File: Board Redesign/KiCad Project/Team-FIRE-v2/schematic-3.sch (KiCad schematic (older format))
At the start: 6 parts, among them IC2 BTS500601TEAAUMA2, J6 U.FL-R-SMT_10_, J7 132136RP, U6 MCP1826T-3302E_DC, U8 TPS82140SILR

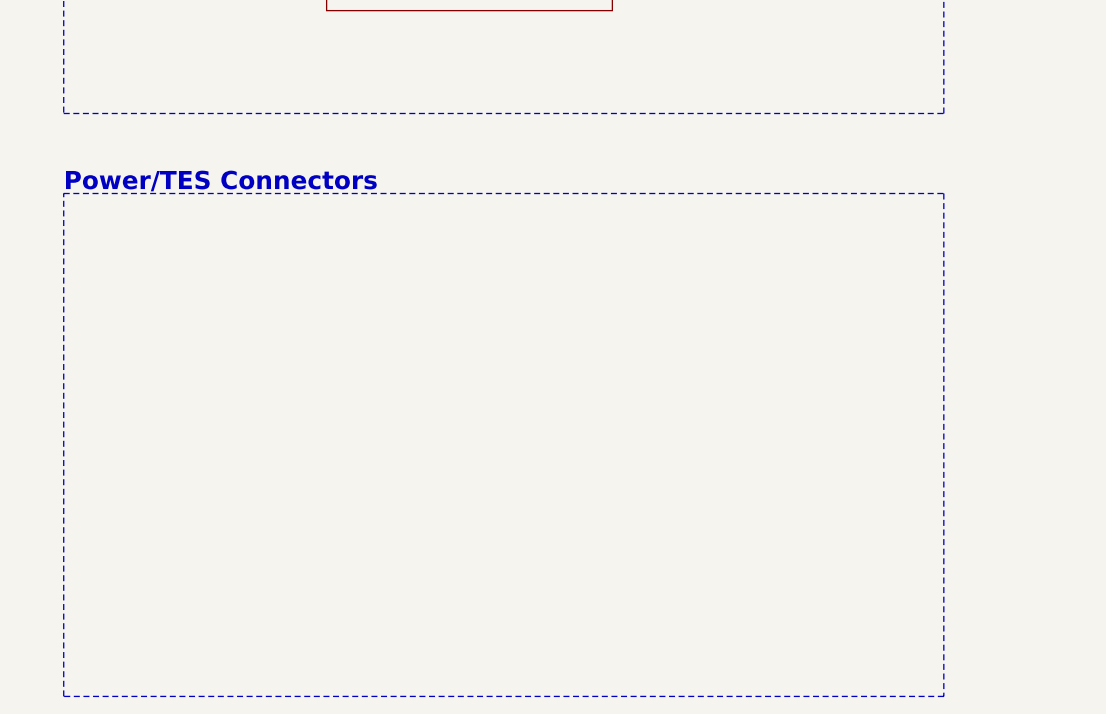
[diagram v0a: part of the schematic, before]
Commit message: Added TES connector
- Added the two 1x3 connectors to page 3 of the schematic
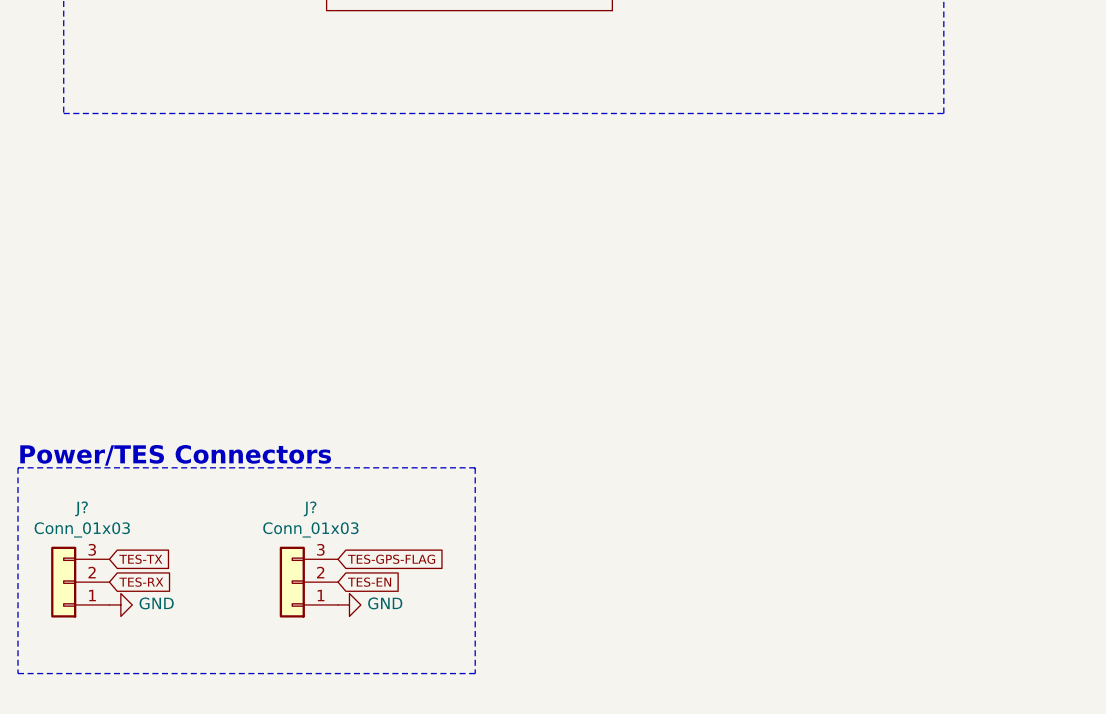
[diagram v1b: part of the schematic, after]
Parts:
- added J? (x2): Conn_01x03, Connector_JST:JST_SH_SM03B-SRSS-TB_1x03-1MP_P1.00mm_Horizontal, symbol Connector_Generic:Conn_01x03
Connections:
- net labels added: TES-EN, TES-GPS-FLAG, TES-RX, TES-TX
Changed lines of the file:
@@
 EESchema Schematic File Version 4
+LIBS:Team-FIRE-v2-cache
 EELAYER 30 0
 EELAYER END
@@
 Text Notes 1050 1000 0    79   ~ 16
 Iridium 8V PMIC
-Wire Notes Line
-	1050 5300 4900 5300
-Wire Notes Line
-	4900 5300 4900 7500
-Wire Notes Line
-	4900 7500 1050 7500
-Wire Notes Line
-	1050 7500 1050 5300
-Text Notes 1050 5300 0    79   ~ 16
+Text Notes 850  6500 0    79   ~ 16
 Power/TES Connectors
 Wire Notes Line
@@
 	1    0    0    -1
 $EndComp
+$Comp
+L Connector_Generic:Conn_01x03 J?
+U 1 1 5EA3E857
+P 1050 7000
+F 0 "J?" H 968 6675 50  0000 C CNN
+F 1 "Conn_01x03" H 968 6766 50  0000 C CNN
+F 2 "Connector_JST:JST_SH_SM03B-SRSS-TB_1x03-1MP_P1.00mm_Horizontal" H 1050 7000 50  0001 C CNN
+F 3 "~" H 1050 7000 50  0001 C CNN
+F 4 "SM03B-SRSS-TB(LF)(SN)" H 1050 7000 50  0001 C CNN "MPN"
+	1    1050 7000
+	-1   0    0    1
+$EndComp
+$Comp
+L Connector_Generic:Conn_01x03 J?
+U 1 1 5EA3FD2C
+P 2050 7000
+F 0 "J?" H 1968 6675 50  0000 C CNN
+F 1 "Conn_01x03" H 1968 6766 50  0000 C CNN
+F 2 "Connector_JST:JST_SH_SM03B-SRSS-TB_1x03-1MP_P1.00mm_Horizontal" H 2050 7000 50  0001 C CNN
+F 3 "~" H 2050 7000 50  0001 C CNN
+F 4 "SM03B-SRSS-TB(LF)(SN)" H 2050 7000 50  0001 C CNN "MPN"
+	1    2050 7000
+	-1   0    0    1
+$EndComp
+Text GLabel 1250 6900 2    39   Input ~ 0
+TES-TX
+Text GLabel 1250 7000 2    39   Input ~ 0
+TES-RX
+$Comp
+L power:GND #PWR?
+U 1 1 5EA4D0AF
+P 1250 7100
+F 0 "#PWR?" H 1250 6850 50  0001 C CNN
+F 1 "GND" V 1255 6972 50  0000 R CNN
+F 2 "" H 1250 7100 50  0001 C CNN
+F 3 "" H 1250 7100 50  0001 C CNN
+	1    1250 7100
+	0    -1   -1   0
+$EndComp
+Text GLabel 2250 6900 2    39   Input ~ 0
+TES-GPS-FLAG
+Text GLabel 2250 7000 2    39   Input ~ 0
+TES-EN
+$Comp
+L power:GND #PWR?
+U 1 1 5EA5A5FD
+P 2250 7100
+F 0 "#PWR?" H 2250 6850 50  0001 C CNN
+F 1 "GND" V 2255 6972 50  0000 R CNN
+F 2 "" H 2250 7100 50  0001 C CNN
+F 3 "" H 2250 7100 50  0001 C CNN
+	1    2250 7100
+	0    -1   -1   0
+$EndComp
+Wire Notes Line
+	850  6500 2850 6500
+Wire Notes Line
+	850  7400 2850 7400
+Wire Notes Line
+	850  6500 850  7400
+Wire Notes Line
+	2850 6500 2850 7400
 $EndSCHEMATC

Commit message: Finished RF Connector
- Deleted old 132136RP antenna connector
- Added new MMCX antenna connector footprint, symbol, and 3D model
- Added MMCX antenna and U.FL connector to Schematic Page 3
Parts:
- removed J6: U.FL-R-SMT_10_, UFLRSMT10, symbol Team-FIRE:U.FL-R-SMT_10_
- removed J7: 132136RP, 132136RP, symbol Team-FIRE:132136RP
- added J?: U.FL-R-SMT_10_, Team-FIRE:UFLRSMT10, symbol Team-FIRE:U.FL-R-SMT_10_
- added J?: PCB.MMCX.F.ST.SMT.JACK.HT, Team-FIRE:PCBMMCXFSTSMTJACKHT, symbol Team-FIRE:PCB.MMCX.F.ST.SMT.JACK.HT
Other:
- note added: "Antenna Connector\n"
- note added: "IRIDIUM U.FL Connector"
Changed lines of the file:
@@
 EESchema Schematic File Version 4
-LIBS:Team-FIRE-v2-cache
 EELAYER 30 0
 EELAYER END
 $Descr A4 11693 8268
 encoding utf-8
-Sheet 4 4
+Sheet 1 1
 Title "Team FIRE Flight-Ready Iridium Carrier"
 Date "2020-02-24"
@@
 Comment4 "Koffi Anderson, Collin Heist, Shelby Linafelter"
 $EndDescr
-Wire Notes Line
-	8250 4750 8250 6050
-Wire Notes Line
-	10850 6050 10850 4750
-Text Notes 8300 4750 0    79   ~ 16
+Text Notes 8350 5200 0    79   ~ 16
 RF Connector
 Text Notes 6850 850  0    79   ~ 16
@@
 Wire Notes Line
 	10700 850  6850 850
-Wire Wire Line
-	9800 5550 9700 5550
-Wire Wire Line
-	9700 5550 9700 5650
-Wire Wire Line
-	9700 5650 9800 5650
-Wire Wire Line
-	9700 5650 9700 5750
-Connection ~ 9700 5650
-Wire Wire Line
-	10600 5450 10700 5450
-Wire Wire Line
-	10700 5450 10700 5550
-Wire Wire Line
-	10600 5550 10700 5550
-Connection ~ 10700 5550
-Wire Wire Line
-	10700 5550 10700 5650
-$Comp
-L power:GND #PWR0152
-U 1 1 5EA5E592
-P 10700 5650
-F 0 "#PWR0152" H 10700 5400 50  0001 C CNN
-F 1 "GND" H 10705 5477 50  0000 C CNN
-F 2 "" H 10700 5650 50  0001 C CNN
-F 3 "" H 10700 5650 50  0001 C CNN
-	1    10700 5650
-	1    0    0    -1
-$EndComp
-$Comp
-L power:GND #PWR0153
-U 1 1 5EA5E7F7
-P 9700 5750
-F 0 "#PWR0153" H 9700 5500 50  0001 C CNN
-F 1 "GND" H 9705 5577 50  0000 C CNN
-F 2 "" H 9700 5750 50  0001 C CNN
-F 3 "" H 9700 5750 50  0001 C CNN
-	1    9700 5750
-	1    0    0    -1
-$EndComp
-$Comp
-L Team-FIRE:U.FL-R-SMT_10_ J6
-U 1 1 5EA5F3F4
-P 9600 5450
-F 0 "J6" H 10150 5085 50  0000 C CNN
-F 1 "U.FL-R-SMT_10_" H 10150 5086 50  0001 C CNN
-F 2 "UFLRSMT10" H 10550 5550 50  0001 L CNN
-F 3 "https://media.digikey.com/pdf/Data%20Sheets/Hirose%20PDFs/UFL%20Series.pdf" H 10550 5450 50  0001 L CNN
-F 4 "RF Connectors / Coaxial Connectors U.FL RECEPTACLE SMT GLD M CONT REEL" H 10550 5350 50  0001 L CNN "Description"
-F 5 "1.25" H 10550 5250 50  0001 L CNN "Height"
-F 6 "Hirose" H 10550 5150 50  0001 L CNN "Manufacturer_Name"
-F 7 "U.FL-R-SMT(10)" H 10150 5176 50  0000 C CNN "MPN"
-F 8 "798-U.FL-R-SMT10" H 10550 4950 50  0001 L CNN "Mouser Part Number"
-F 9 "https://www.mouser.com/Search/Refine.aspx?Keyword=798-U.FL-R-SMT10" H 10550 4850 50  0001 L CNN "Mouser Price/Stock"
-	1    9600 5450
-	-1   0    0    1
-$EndComp
-$Comp
-L Team-FIRE:132136RP J7
-U 1 1 5EA604BA
-P 9800 5450
-F 0 "J7" H 10200 5715 50  0000 C CNN
-F 1 "132136RP" H 10200 5714 50  0001 C CNN
-F 2 "132136RP" H 10450 5550 50  0001 L CNN
-F 3 "https://componentsearchengine.com/Datasheets/2/132136RP.pdf" H 10450 5450 50  0001 L CNN
-F 4 "RF Connectors / Coaxial Connectors" H 10450 5350 50  0001 L CNN "Description"
-F 5 "9.86" H 10450 5250 50  0001 L CNN "Height"
-F 6 "Amphenol" H 10450 5150 50  0001 L CNN "Manufacturer_Name"
-F 7 "523-132136RP" H 10450 4950 50  0001 L CNN "Mouser Part Number"
-F 8 "https://www.mouser.com/Search/Refine.aspx?Keyword=523-132136RP" H 10450 4850 50  0001 L CNN "Mouser Price/Stock"
-F 9 "70032830" H 10450 4550 50  0001 L CNN "Allied_Number"
-F 10 "https://www.alliedelec.com/amphenolrf-132136rp/70032830/" H 10450 4450 50  0001 L CNN "Allied Price/Stock"
-F 11 "132136RP" H 10200 5624 50  0000 C CNN "MPN"
-	1    9800 5450
-	1    0    0    -1
-$EndComp
-Wire Wire Line
-	9600 5450 9800 5450
-$Comp
-L power:GND #PWR0154
-U 1 1 5EA632DA
-P 8400 5550
-F 0 "#PWR0154" H 8400 5300 50  0001 C CNN
-F 1 "GND" H 8405 5377 50  0000 C CNN
-F 2 "" H 8400 5550 50  0001 C CNN
-F 3 "" H 8400 5550 50  0001 C CNN
-	1    8400 5550
-	1    0    0    -1
-$EndComp
-Wire Wire Line
-	8500 5450 8400 5450
-Wire Wire Line
-	8400 5450 8400 5350
-Wire Wire Line
-	8400 5350 8500 5350
-Wire Wire Line
-	8400 5450 8400 5550
-Connection ~ 8400 5450
-Wire Notes Line
-	8250 4750 10850 4750
-Wire Notes Line
-	10850 6050 8250 6050
+Wire Notes Line
+	8300 5200 10900 5200
+Wire Notes Line
+	10900 6300 8300 6300
 Wire Notes Line
 	4900 3200 1050 3200
@@
 Wire Notes Line
 	2850 6500 2850 7400
+$Comp
+L Team-FIRE:U.FL-R-SMT_10_ J?
+U 1 1 5EA3C18D
+P 9650 5700
+F 0 "J?" H 10200 5427 50  0000 C CNN
+F 1 "U.FL-R-SMT_10_" H 10200 5426 50  0001 C CNN
+F 2 "Team-FIRE:UFLRSMT10" H 10600 5800 50  0001 L CNN
+F 3 "https://media.digikey.com/pdf/Data%20Sheets/Hirose%20PDFs/UFL%20Series.pdf" H 10600 5700 50  0001 L CNN
+F 4 "RF Connectors / Coaxial Connectors U.FL RECEPTACLE SMT GLD M CONT REEL" H 10600 5600 50  0001 L CNN "Description"
+F 5 "1.25" H 10600 5500 50  0001 L CNN "Height"
+F 6 "Hirose" H 10600 5400 50  0001 L CNN "Manufacturer_Name"
+F 7 "U.FL-R-SMT(10)" H 10600 5300 50  0001 L CNN "Manufacturer_Part_Number"
+F 8 "798-U.FL-R-SMT10" H 10600 5200 50  0001 L CNN "MPN"
+F 9 "https://www.mouser.com/Search/Refine.aspx?Keyword=798-U.FL-R-SMT10" H 10600 5100 50  0001 L CNN "Mouser Price/Stock"
+	1    9650 5700
+	-1   0    0    1
+$EndComp
+$Comp
+L Team-FIRE:PCB.MMCX.F.ST.SMT.JACK.HT J?
+U 1 1 5EA3CD82
+P 9750 5700
+F 0 "J?" H 10150 5873 50  0000 C CNN
+F 1 "PCB.MMCX.F.ST.SMT.JACK.HT" H 10150 5874 50  0001 C CNN
+F 2 "Team-FIRE:PCBMMCXFSTSMTJACKHT" H 10400 5800 50  0001 L CNN
+F 3 "https://www.mouser.mx/datasheet/2/398/PCB.MMCX.F.ST.SMT.JACK.HT-29444.pdf" H 10400 5700 50  0001 L CNN
+F 4 "RF Connectors / Coaxial Connectors MMCX Straight SMT Mount for PCB" H 10400 5600 50  0001 L CNN "Description"
+F 5 "4.34" H 10400 5500 50  0001 L CNN "Height"
+F 6 "Taoglas" H 10400 5400 50  0001 L CNN "Manufacturer_Name"
+F 7 "PCB.MMCX.F.ST.SMT.JACK.HT" H 10400 5300 50  0001 L CNN "MPN"
+F 8 "960-PCBMMCXFSTJACKHT" H 10400 5200 50  0001 L CNN "Mouser Part Number"
+F 9 "https://www.mouser.com/Search/Refine.aspx?Keyword=960-PCBMMCXFSTJACKHT" H 10400 5100 50  0001 L CNN "Mouser Price/Stock"
+	1    9750 5700
+	1    0    0    -1
+$EndComp
+Wire Wire Line
+	10550 5700 10650 5700
+Wire Wire Line
+	10650 5700 10650 5800
+Wire Wire Line
+	10550 5800 10650 5800
+Connection ~ 10650 5800
+Wire Wire Line
+	10650 5800 10650 6000
+Wire Wire Line
+	8550 5600 8450 5600
+Wire Wire Line
+	8450 5600 8450 5700
+Wire Wire Line
+	8550 5700 8450 5700
+Connection ~ 8450 5700
+Wire Wire Line
+	8450 5700 8450 6000
+Wire Wire Line
+	9650 5700 9750 5700
+Wire Wire Line
+	9750 5800 9650 5800
+Wire Wire Line
+	9650 5800 9650 5900
+Wire Wire Line
+	9750 5900 9650 5900
+Connection ~ 9650 5900
+Wire Wire Line
+	9650 5900 9650 6000
+$Comp
+L power:GND #PWR?
+U 1 1 5EA3F8A4
+P 8450 6000
+F 0 "#PWR?" H 8450 5750 50  0001 C CNN
+F 1 "GND" H 8455 5827 50  0000 C CNN
+F 2 "" H 8450 6000 50  0001 C CNN
+F 3 "" H 8450 6000 50  0001 C CNN
+	1    8450 6000
+	1    0    0    -1
+$EndComp
+$Comp
+L power:GND #PWR?
+U 1 1 5EA3FB3C
+P 9650 6000
+F 0 "#PWR?" H 9650 5750 50  0001 C CNN
+F 1 "GND" H 9655 5827 50  0000 C CNN
+F 2 "" H 9650 6000 50  0001 C CNN
+F 3 "" H 9650 6000 50  0001 C CNN
+	1    9650 6000
+	1    0    0    -1
+$EndComp
+$Comp
+L power:GND #PWR?
+U 1 1 5EA3FD51
+P 10650 6000
+F 0 "#PWR?" H 10650 5750 50  0001 C CNN
+F 1 "GND" H 10655 5827 50  0000 C CNN
+F 2 "" H 10650 6000 50  0001 C CNN
+F 3 "" H 10650 6000 50  0001 C CNN
+	1    10650 6000
+	1    0    0    -1
+$EndComp
+Text Notes 8700 5350 0    50   ~ 0
+IRIDIUM U.FL Connector
+Text Notes 9850 5500 0    50   ~ 0
+Antenna Connector\n
+Wire Notes Line
+	10900 5200 10900 6300
+Wire Notes Line
+	8300 6300 8300 5200
 $EndSCHEMATC

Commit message: Finished PMICs
- Finished stuff on schematic page 3!
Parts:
- added C?: 1u, Capacitor_SMD:C_0805_2012Metric, symbol Device:C
- added R? (x2): 10k, Resistor_SMD:R_0603_1608Metric, symbol Device:R
- added R? (x2): 1k, Resistor_SMD:R_0603_1608Metric, symbol Device:R
- IC2: footprint BTS500601TEAAUMA2 -> Team-FIRE:BTS500601TEAAUMA2; symbol BTS500601TEAAUMA2:BTS500601TEAAUMA2 -> Team-FIRE:BTS500601TEAAUMA2; MPN (none) -> BTS500601TEAAUMA2; Manufacturer_Part_Number BTS500601TEAAUMA2 -> (none)
- J?: symbol Team-FIRE:U.FL-R-SMT_10_ -> Team-FIRE-v2-rescue:U.FL-R-SMT_10_-Team-FIRE
- U?: renamed from U6; footprint SOT-223_5MC_MCH -> Package_TO_SOT_SMD:SOT-223-5; symbol 5_to_3.3_linreg:MCP1826T-3302E_DC -> Team-FIRE:MCP1826T-3302E_DC
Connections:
- net GND: now also IC2.1 (GND), U?.3 (GND), C?.2, R?.2
- net TES-EN: now also U?.1 (*SHDN)
- net at IC2.2 (IN): now also R?.1
- net IR_BOOST: now reaches IC2.3 (OUT)
- net at IC2.4 (IS): now also R?.1, R?.1
- net VBAT: now reaches IC2.5 (VS)
- net +5V: now reaches U?.2 (VIN)
- net +3V3: now reaches U?.4 (VOUT)
- net +3V3: now also C?.1, R?.1
- net at U?.5 (PWRGD): now also R?.2
- new net 8V_EN: R?.2
- new net 8V_ISENSE: R?.2
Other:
- moved on the sheet: IC2, U?

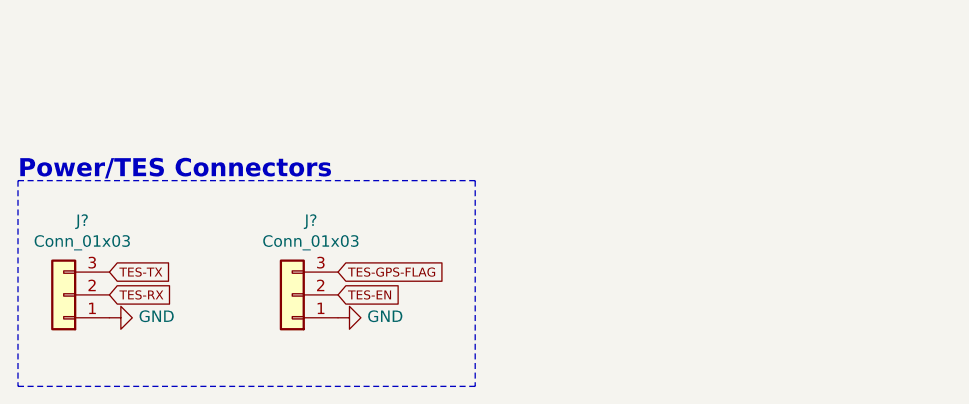
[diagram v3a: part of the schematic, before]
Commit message: Progress
- Corrected many footprint errors on components
- Finalized work on schematic 3
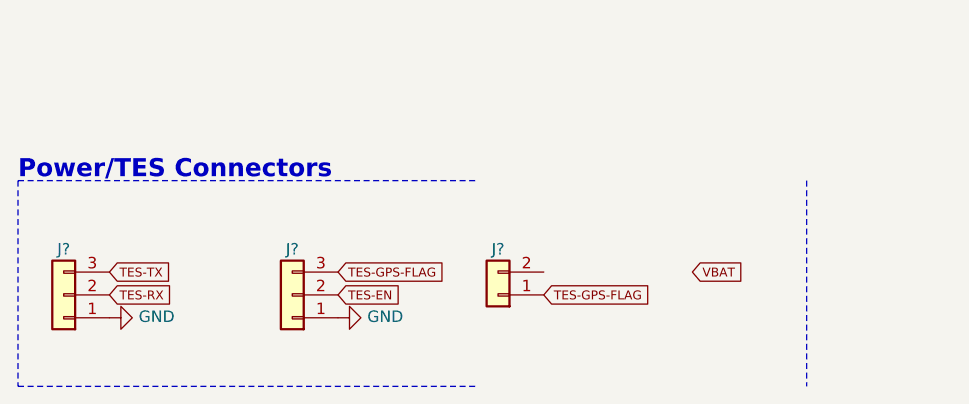
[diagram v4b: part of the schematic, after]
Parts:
- added J?: Conn_01x02, Team-FIRE:43650-0200, symbol Connector_Generic:Conn_01x02
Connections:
- net TES-GPS-FLAG: now also J?.1 (Pin_1)
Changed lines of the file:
@@
 U 1 1 5EA3E857
 P 1050 7000
-F 0 "J?" H 968 6675 50  0000 C CNN
-F 1 "Conn_01x03" H 968 6766 50  0000 C CNN
+F 0 "J?" H 1050 6800 50  0000 C CNN
+F 1 "Conn_01x03" H 968 6766 50  0001 C CNN
 F 2 "Connector_JST:JST_SH_SM03B-SRSS-TB_1x03-1MP_P1.00mm_Horizontal" H 1050 7000 50  0001 C CNN
 F 3 "~" H 1050 7000 50  0001 C CNN
@@
 U 1 1 5EA3FD2C
 P 2050 7000
-F 0 "J?" H 1968 6675 50  0000 C CNN
-F 1 "Conn_01x03" H 1968 6766 50  0000 C CNN
+F 0 "J?" H 2050 6800 50  0000 C CNN
+F 1 "Conn_01x03" H 1968 6766 50  0001 C CNN
 F 2 "Connector_JST:JST_SH_SM03B-SRSS-TB_1x03-1MP_P1.00mm_Horizontal" H 2050 7000 50  0001 C CNN
 F 3 "~" H 2050 7000 50  0001 C CNN
@@
 	850  6500 850  7400
 Wire Notes Line
-	2850 6500 2850 7400
+	4300 6500 4300 7400
 $Comp
 L Team-FIRE-v2-rescue:U.FL-R-SMT_10_-Team-FIRE J?
@@
 Wire Notes Line
 	1000 4800 1000 3450
+$Comp
+L Connector_Generic:Conn_01x02 J?
+U 1 1 5EB75BFF
+P 2950 7000
+F 0 "J?" H 2950 6800 50  0000 C CNN
+F 1 "Conn_01x02" H 2868 6766 50  0001 C CNN
+F 2 "Team-FIRE:43650-0200" H 2950 7000 50  0001 C CNN
+F 3 "~" H 2950 7000 50  0001 C CNN
+F 4 "43650-0200" H 2950 7000 50  0001 C CNN "MPN"
+	1    2950 7000
+	-1   0    0    1
+$EndComp
+Text GLabel 3800 6900 2    39   Input ~ 0
+VBAT
+Text GLabel 3150 7000 2    39   Input ~ 0
+TES-GPS-FLAG
 $EndSCHEMATC

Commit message: Buck Converter & Test Points
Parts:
- added C?: 10uF, Capacitor_SMD:C_0805_2012Metric, symbol Device:C
- added C?: 430pF, Capacitor_SMD:C_0805_2012Metric, symbol Device:C
- added C?: 47uF, Capacitor_SMD:C_0805_2012Metric, symbol Device:C
- added R? (x2): 100k, Resistor_SMD:R_0603_1608Metric, symbol Device:R
- added R?: 523k, Resistor_SMD:R_0603_1608Metric, symbol Device:R
- added TP? (x7): TestPoint, symbol Connector:TestPoint
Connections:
- net +3V3: now also TP?.1
- net +5V: now also U8.4 (VOUT), U8.5 (VOUT), C?.1, R?.1, R?.2, TP?.1
- net GND: now also U8.3 (GND), U8.9 (PAD), C?.2, C?.2, C?.2, R?.1
- net VBAT: now also J?.2 (Pin_2), U8.1 (EN), U8.2 (VIN), C?.1
- net EN_IR_BUS: now reaches TP1.1
- net at U8.6 (FB): now also R?.1, R?.2
- net at U8.7 (PG): now also R?.2
- net at U8.8 (SS_TR): now also C?.1
- new net BOOST_EN: TP?.1
- new net IR_SIM_EN: TP?.1
- new net PWR_EN: TP?.1
- new net RF_EN: TP?.1
- new net TX_ACTIVE: TP?.1
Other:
- moved on the sheet: C?, J?, R?, TP1, U8, U?
